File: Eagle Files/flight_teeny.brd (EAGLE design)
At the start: 46.4 x 34.9 mm, 21 parts, among them M4 WIRELESS-NRF24L01, Q1 SI2302, Q2 SI2302, Q3 SI2302, Q5 SI2302, U2 GY-521MPU6050

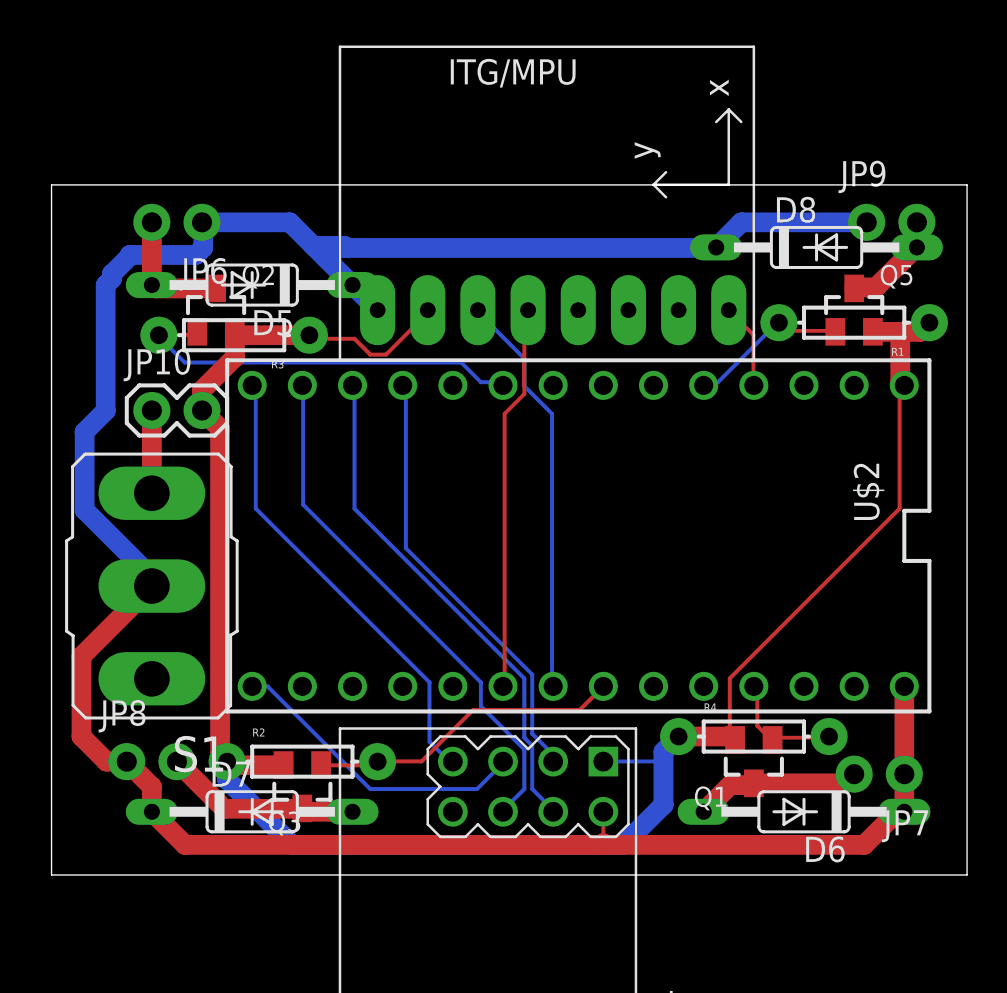
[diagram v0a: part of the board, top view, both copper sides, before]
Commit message: Changed power supply for mrf and mpu. Corrected of overlaping pads
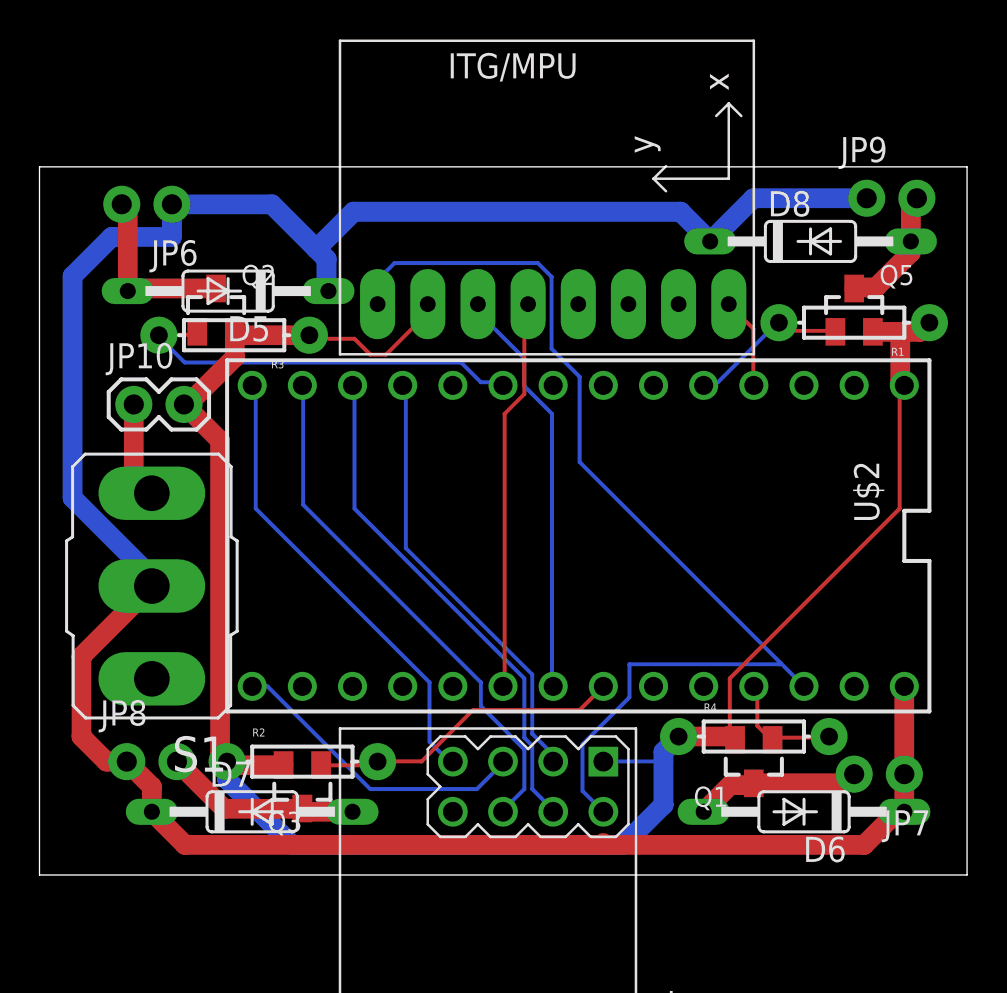
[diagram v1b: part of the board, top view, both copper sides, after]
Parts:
- moved JP6 1.78 mm to (29.0, 49.8)
- moved D5 1.26 mm to (31.8, 45.4)
- moved JP9 1.22 mm to (64.1, 50.1)
- moved JP10 0.96 mm to (27.0, 39.7)
- moved D8 0.43 mm to (61.3, 47.9)
- moved U2 0.30 mm to (48.3, 53.6)
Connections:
- removed net N$10: U$2.3.3V
- new net 3.3V: M4.2, U$2.3.3V, U2.VCC
- net P_IN: no longer M4.2, U2.VCC
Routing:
- net 3.3V: track 0.00 -> 53.3 mm
- net N$21: track 6.60 -> 9.15 mm
- net GND: track 103.8 -> 105.2 mm
- net N$15: track 5.30 -> 6.49 mm
- net P_IN: track 134.3 -> 133.3 mm
- net N$30: track 4.19 -> 4.87 mm
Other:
- board size 46.4 x 34.9 mm -> 47 x 35.9 mm

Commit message: PWM pin corrected. Shifted from 7 to 6
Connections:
- removed net N$3: U$2.6
- new net 7: U$2.7
- net PWM3: now also U$2.6; no longer U$2.7
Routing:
- net PWM3: track 20.6 -> 24.3 mm
- net A5: track 21.1 -> 23.5 mm
- net 3.3V: track 53.3 -> 55.0 mm
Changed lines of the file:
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@@
 <contactref element="U2" pad="SCL"/>
 <contactref element="U$2" pad="19/A5"/>
-<wire x1="48.2" y1="39.2" x2="48.2" y2="25.4" width="0.2" layer="16"/>
-<wire x1="46.8" y1="40.6" x2="48.2" y2="39.2" width="0.2" layer="16"/>
-<wire x1="46.8" y1="42" x2="46.8" y2="40.6" width="0.2" layer="16"/>
-<wire x1="44.2476" y1="44.5524" x2="46.8" y2="42" width="0.2" layer="16"/>
 <wire x1="48.2" y1="25.4" x2="48.26" y2="25.4" width="0.2" layer="16"/>
-<wire x1="44.2476" y1="44.5524" x2="44.45" y2="44.7548" width="0.2" layer="16"/>
+<wire x1="48.689375" y1="41.9814" x2="49.6014" y2="41.069375" width="0.2" layer="16"/>
+<wire x1="49.6014" y1="41.069375" x2="49.6014" y2="39.905825" width="0.2" layer="16"/>
+<wire x1="48.2" y1="38.504425" x2="48.2" y2="25.4" width="0.2" layer="16"/>
+<wire x1="49.6014" y1="39.905825" x2="48.2" y2="38.504425" width="0.2" layer="16"/>
+<wire x1="44.45" y1="44.7548" x2="45.4152" y2="43.7896" width="0.2" layer="16"/>
+<wire x1="45.4152" y1="43.7896" x2="45.4152" y2="42.9768" width="0.2" layer="16"/>
+<wire x1="45.4152" y1="42.9768" x2="46.4106" y2="41.9814" width="0.2" layer="16"/>
+<wire x1="46.4106" y1="41.9814" x2="48.689375" y2="41.9814" width="0.2" layer="16"/>
 </signal>
 <signal name="D2">
@@
 <contactref element="Q2" pad="1"/>
 <contactref element="R3" pad="P$2"/>
-<contactref element="U$2" pad="7"/>
 <wire x1="28.4" y1="43.2" x2="30.2" y2="43.2" width="0.2" layer="1"/>
 <wire x1="30.2" y1="43.2" x2="30.2412" y2="43.35" width="0.2" layer="1"/>
 <wire x1="28.4" y1="43.2" x2="28.2956" y2="43.18" width="0.2" layer="1"/>
-<wire x1="44.6" y1="40.8" x2="45.6" y2="40.8" width="0.2" layer="16"/>
-<wire x1="43.6" y1="41.8" x2="44.6" y2="40.8" width="0.2" layer="16"/>
-<wire x1="29.6" y1="41.8" x2="43.6" y2="41.8" width="0.2" layer="16"/>
+<wire x1="43.6" y1="41.8" x2="29.6" y2="41.8" width="0.2" layer="16"/>
 <wire x1="28.4" y1="43" x2="29.6" y2="41.8" width="0.2" layer="16"/>
-<wire x1="45.6" y1="40.8" x2="45.72" y2="40.64" width="0.2" layer="16"/>
 <wire x1="28.4" y1="43" x2="28.2956" y2="43.18" width="0.2" layer="16"/>
+<contactref element="U$2" pad="6"/>
+<wire x1="46.149375" y1="39.6034" x2="45.290625" y2="39.6034" width="0.2" layer="16"/>
+<wire x1="48.26" y1="40.64" x2="47.185975" y2="40.64" width="0.2" layer="16"/>
+<wire x1="47.185975" y1="40.64" x2="46.149375" y2="39.6034" width="0.2" layer="16"/>
+<wire x1="45.290625" y1="39.6034" x2="44.2166" y2="40.677425" width="0.2" layer="16"/>
+<wire x1="44.2166" y1="40.677425" x2="44.2166" y2="41.069375" width="0.2" layer="16"/>
+<wire x1="43.6" y1="41.685975" x2="43.6" y2="41.8" width="0.2" layer="16"/>
+<wire x1="44.2166" y1="41.069375" x2="43.6" y2="41.685975" width="0.2" layer="16"/>
 </signal>
 <signal name="P_IN">
@@
 <contactref element="M4" pad="2"/>
 <contactref element="U2" pad="VCC"/>
-<wire x1="47.4825" y1="46.8328" x2="48.179" y2="46.1363" width="0.2" layer="16"/>
-<wire x1="49.6014" y1="36.7586" x2="59.7916" y2="26.5684" width="0.2" layer="16"/>
+<wire x1="52.0398" y1="34.3202" x2="59.7916" y2="26.5684" width="0.2" layer="16"/>
 <wire x1="59.7916" y1="26.5684" x2="60.96" y2="25.4" width="0.2" layer="16"/>
-<wire x1="49.6014" y1="41.069375" x2="49.6014" y2="36.7586" width="0.2" layer="16"/>
-<wire x1="47.4825" y1="46.8328" x2="40.2288" y2="46.8328" width="0.2" layer="16"/>
-<wire x1="40.2288" y1="46.8328" x2="39.37" y2="45.974" width="0.2" layer="16"/>
+<wire x1="39.37" y1="45.974" x2="40.2288" y2="46.8328" width="0.2" layer="16"/>
 <wire x1="39.37" y1="44.7548" x2="39.37" y2="45.974" width="0.2" layer="16"/>
-<wire x1="48.179" y1="42.491775" x2="49.6014" y2="41.069375" width="0.2" layer="16"/>
-<wire x1="48.179" y1="46.1363" x2="48.179" y2="42.491775" width="0.2" layer="16"/>
 <wire x1="52.1208" y1="24.8430625" x2="52.1208" y2="26.5176" width="0.2" layer="16"/>
 <wire x1="52.1208" y1="24.8430625" x2="49.746" y2="22.4682625" width="0.2" layer="16"/>
@@
 <wire x1="49.746" y1="20.104" x2="50.8" y2="19.05" width="0.2" layer="16"/>
 <wire x1="49.746" y1="22.4682625" x2="49.746" y2="20.104" width="0.2" layer="16"/>
+<wire x1="50.3984" y1="46.8328" x2="50.881" y2="46.3502" width="0.2" layer="16"/>
+<wire x1="50.881" y1="46.3502" x2="50.881" y2="42.6926" width="0.2" layer="16"/>
+<wire x1="50.881" y1="42.6926" x2="52.0398" y2="41.5338" width="0.2" layer="16"/>
+<wire x1="52.0398" y1="41.5338" x2="52.0398" y2="34.3202" width="0.2" layer="16"/>
+<wire x1="40.2288" y1="46.8328" x2="50.3984" y2="46.8328" width="0.2" layer="16"/>
 </signal>
 <signal name="D9">
@@
 <contactref element="U$2" pad="5"/>
 </signal>
-<signal name="N$3">
-<contactref element="U$2" pad="6"/>
+<signal name="7">
+<contactref element="U$2" pad="7"/>
 </signal>
 </signals>

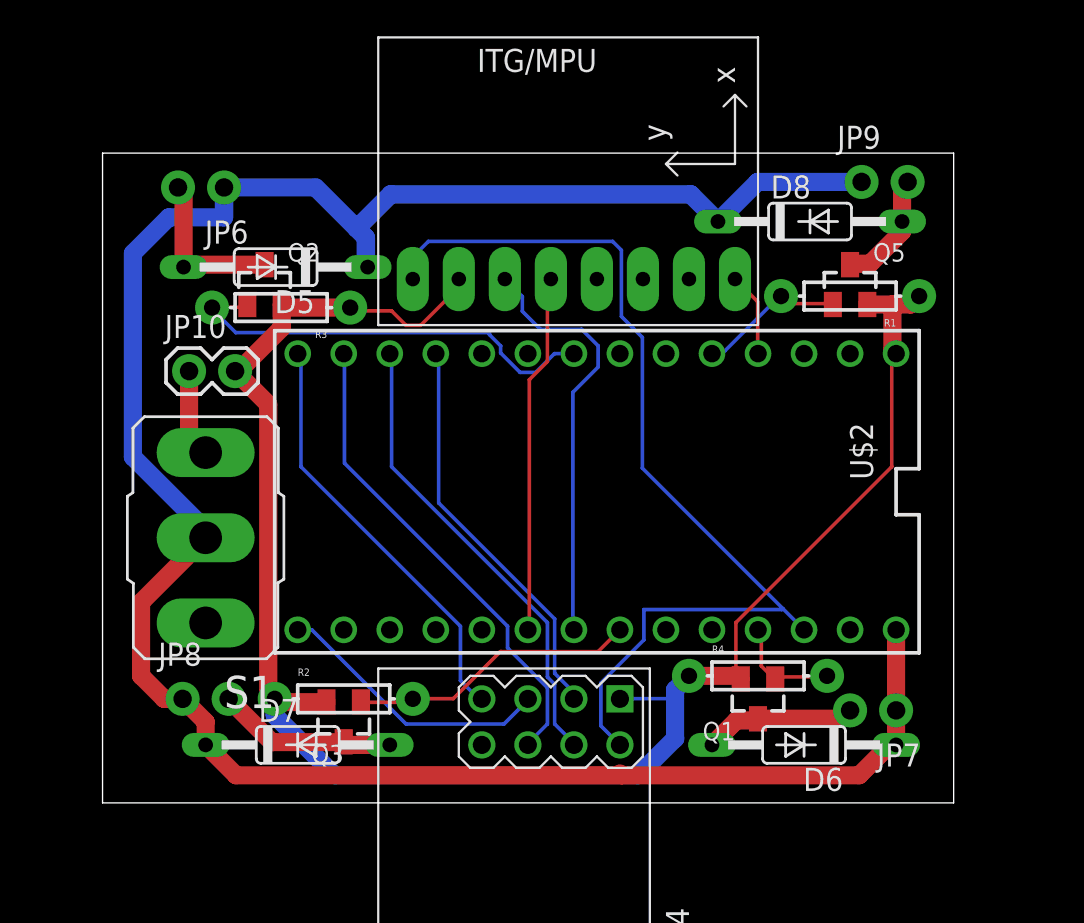
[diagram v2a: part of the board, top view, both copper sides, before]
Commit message: Added holes
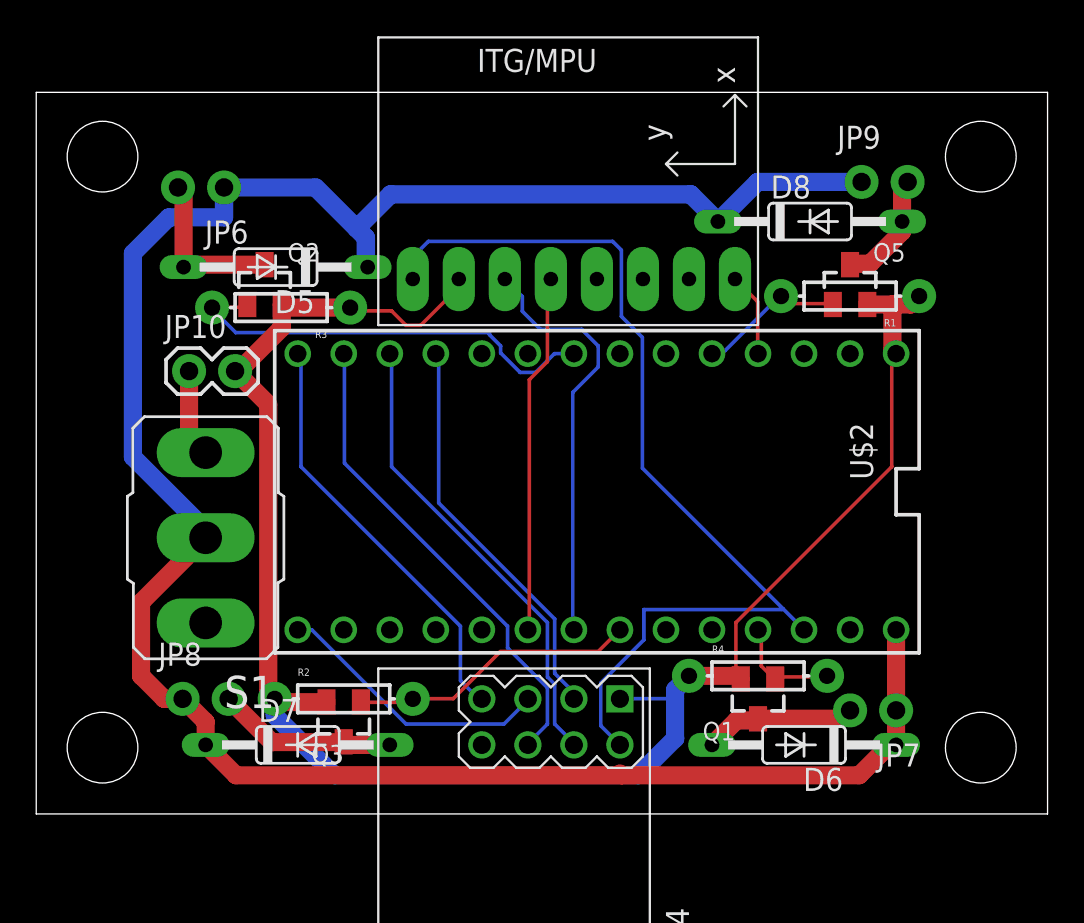
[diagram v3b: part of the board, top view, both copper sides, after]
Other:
- board size 47 x 35.9 mm -> 55.8 x 39.8 mm
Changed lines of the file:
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@@
 <board>
 <plain>
-<wire x1="22.2504" y1="15.8496" x2="69.2152" y2="15.8496" width="0" layer="20"/>
-<wire x1="69.2152" y1="15.8496" x2="69.2152" y2="51.7044" width="0" layer="20"/>
-<wire x1="69.2152" y1="51.7044" x2="22.2504" y2="51.7044" width="0" layer="20"/>
-<wire x1="22.2504" y1="51.7044" x2="22.2504" y2="15.8496" width="0" layer="20"/>
+<wire x1="18.5928" y1="15.24" x2="74.3968" y2="15.24" width="0" layer="20"/>
+<wire x1="74.3968" y1="15.24" x2="74.3968" y2="55.0572" width="0" layer="20"/>
+<wire x1="74.3968" y1="55.0572" x2="18.5928" y2="55.0572" width="0" layer="20"/>
+<wire x1="18.5928" y1="55.0572" x2="18.5928" y2="15.24" width="0" layer="20"/>
+<hole x="70.7136" y="51.5112" drill="3.9"/>
+<hole x="22.2504" y="51.5112" drill="3.9"/>
+<hole x="70.7136" y="18.8976" drill="3.9"/>
+<hole x="22.2504" y="18.8976" drill="3.9"/>
 </plain>
 <attributes>

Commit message: PCB Shape Added
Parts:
- moved Q5 57.4 mm to (17.2, 10.6)
- moved JP7 56.9 mm to (20.3, -12.9)
- moved M4 56.9 mm to (-1.27, -24.9)
- moved D5 56.9 mm to (-13.9, 11.6)
- moved D6 56.9 mm to (15.2, -14.8)
- moved D7 56.9 mm to (-12.7, -14.8)
- moved D8 56.9 mm to (15.6, 14.1)
- moved JP10 56.9 mm to (-18.7, 5.84)
- moved JP6 56.9 mm to (-16.8, 16.0)
- moved JP8 56.9 mm to (-19.1, -12.2)
- moved Q1 56.9 mm to (12.7, -12.2)
- moved Q2 56.9 mm to (-14.5, 10.6)
- moved Q3 56.9 mm to (-10.2, -13.5)
- moved R1 56.9 mm to (17.8, 9.98)
- moved R2 56.9 mm to (-10.2, -12.2)
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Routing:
- net P_IN: track 133.3 -> 132.0 mm
- net N$15: track 6.49 -> 7.10 mm
- net GND: track 105.2 -> 105.8 mm
- net PWM1: track 8.17 -> 7.56 mm
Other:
- board size 55.8 x 39.8 mm -> 46 x 50 mm

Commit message: Added Shape and Silkscreen
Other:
- outline, holes or cut-outs redrawn
- board text added: "Mihir Kulkarni Mihir Dharmadhikari Aerodynamics Club BPGC"
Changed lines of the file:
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@@
 <plain>
 <circle x="-15" y="21" radius="2.3" width="0.001" layer="20"/>
+<wire x1="-11" y1="21" x2="-19" y2="21" width="0.001" layer="20" curve="180"/>
 <circle x="15" y="21" radius="2.3" width="0.001" layer="20"/>
+<wire x1="19" y1="21" x2="11" y2="21" width="0.001" layer="20" curve="180"/>
+<wire x1="11" y1="-21" x2="19" y2="-21" width="0.001" layer="20" curve="180"/>
 <circle x="15" y="-21" radius="2.3" width="0.001" layer="20"/>
+<wire x1="-19" y1="-21" x2="-11" y2="-21" width="0.001" layer="20" curve="180"/>
 <circle x="-15" y="-21" radius="2.3" width="0.001" layer="20"/>
-<wire x1="-11" y1="21" x2="-15" y2="25" width="0.001" layer="20" curve="90"/>
-<wire x1="15" y1="25" x2="11" y2="21" width="0.001" layer="20" curve="90"/>
-<wire x1="11" y1="-21" x2="15" y2="-25" width="0.001" layer="20" curve="90"/>
-<wire x1="-15" y1="-25" x2="-11" y2="-21" width="0.001" layer="20" curve="90"/>
-<wire x1="23" y1="20" x2="18" y2="25" width="0.001" layer="20" curve="90"/>
-<wire x1="18" y1="-25" x2="23" y2="-20" width="0.001" layer="20" curve="90"/>
-<wire x1="-23" y1="-20" x2="-18" y2="-25" width="0.001" layer="20" curve="90"/>
-<wire x1="-18" y1="25" x2="-23" y2="20" width="0.001" layer="20" curve="90"/>
-<wire x1="-18" y1="25" x2="-15" y2="25" width="0.001" layer="20"/>
-<wire x1="-23" y1="20" x2="-23" y2="-20" width="0.001" layer="20"/>
-<wire x1="-18" y1="-25" x2="-15" y2="-25" width="0.001" layer="20"/>
-<wire x1="23" y1="20" x2="23" y2="-20" width="0.001" layer="20"/>
-<wire x1="15" y1="25" x2="18" y2="25" width="0.001" layer="20"/>
-<wire x1="15" y1="-25" x2="18" y2="-25" width="0.001" layer="20"/>
+<wire x1="-23" y1="21" x2="-23" y2="-21" width="0.001" layer="20"/>
+<wire x1="23" y1="21" x2="19" y2="21" width="0.001" layer="20"/>
+<wire x1="23" y1="21" x2="23" y2="-21" width="0.001" layer="20"/>
 <wire x1="-11" y1="21" x2="11" y2="21" width="0.001" layer="20"/>
+<wire x1="-23" y1="21" x2="-19" y2="21" width="0.001" layer="20"/>
+<wire x1="-23" y1="-21" x2="-19" y2="-21" width="0.001" layer="20"/>
 <wire x1="-11" y1="-21" x2="11" y2="-21" width="0.001" layer="20"/>
+<wire x1="23" y1="-21" x2="19" y2="-21" width="0.001" layer="20"/>
+<text x="19" y="-4.5" size="1.778" layer="22" font="vector" rot="MR0">Mihir Kulkarni
+Mihir Dharmadhikari
+Aerodynamics Club BPGC</text>
 </plain>
 <attributes>
@@
 </drawing>
 <compatibility>
+<note version="6.3" minversion="6.2.2" severity="warning">
+Since Version 6.2.2 text objects can contain more than one line,
+which will not be processed correctly with this version.
+</note>
 <note version="8.2" severity="warning">
 Since Version 8.2, EAGLE supports online libraries. The ids
